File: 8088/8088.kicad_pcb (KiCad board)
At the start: 2 copper layers, 154.9 x 91.4 mm, 108 parts, among them CON1 BARREL_JACK, U1 8284, U10 2114, U11 ULN2803ADWR, U12 74LS14, U13 ULN2803ADWR, U14 ULN2803ADWR, U15 ULN2803ADWR, U16 7805, U2 8088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

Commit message: Updated libraries. Added IO headers to schematics. TODO: Route ISA bus
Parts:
- removed U3CLK/RDY: CONN_01X02, Pin_Headers:Pin_Header_Straight_1x02_Pitch2.54mm
- moved GND 5.71 mm to (223.0, 55.2)
- moved GND 5.71 mm to (216.7, 55.2)
- moved GND 5.71 mm to (210.2, 55.2)
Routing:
- net 8755-READY: track 6.02 -> 0.00 mm
- net 8755-CLK: track 4.07 -> 0.00 mm
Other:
- outline, holes or cut-outs redrawn
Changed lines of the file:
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@@
-(kicad_pcb (version 4) (host pcbnew 4.0.6)
+(kicad_pcb (version 4) (host pcbnew 4.0.3-stable)
   (general
-    (links 352)
+    (links 353)
     (no_connects 0)
     (area 62.23 19.05 255.270001 151.765001)
     (thickness 1.6)
     (drawings 7)
-    (tracks 1859)
+    (tracks 1855)
     (zones 0)
-    (modules 108)
+    (modules 107)
     (nets 189)
   )
@@
   )
   (module Pin_Headers:Pin_Header_Straight_2x02_Pitch2.54mm (layer F.Cu)
-    (at 223.012 49.53)
+    (at 223.012 55.245)
     (descr "Through hole straight pin header, 2x02, 2.54mm pitch, double rows")
     (tags "Through hole pin header THT 2x02 2.54mm double row")
@@
   )
   (module Pin_Headers:Pin_Header_Straight_2x02_Pitch2.54mm (layer F.Cu)
-    (at 216.662 49.53)
+    (at 216.662 55.245)
     (descr "Through hole straight pin header, 2x02, 2.54mm pitch, double rows")
     (tags "Through hole pin header THT 2x02 2.54mm double row")
@@
     )
   )
-  (module Pin_Headers:Pin_Header_Straight_1x02_Pitch2.54mm (layer F.Cu)
-    (at 139.7 69.85)
-    (descr "Through hole straight pin header, 1x02, 2.54mm pitch, single row")
-    (tags "Through hole pin header THT 1x02 2.54mm single row")
-    (fp_text reference U3CLK/RDY (at -2.54 1.27 90) (layer F.SilkS)
-      (effects (font (size 1 1) (thickness 0.15)))
-    )
-    (fp_text value CONN_01X02 (at 0 4.87) (layer F.Fab) hide
-      (effects (font (size 1 1) (thickness 0.15)))
-    )
-    (fp_line (start -0.635 -1.27) (end 1.27 -1.27) (layer F.Fab) (width 0.1))
-    (fp_line (start 1.27 -1.27) (end 1.27 3.81) (layer F.Fab) (width 0.1))
-    (fp_line (start 1.27 3.81) (end -1.27 3.81) (layer F.Fab) (width 0.1))
-    (fp_line (start -1.27 3.81) (end -1.27 -0.635) (layer F.Fab) (width 0.1))
-    (fp_line (start -1.27 -0.635) (end -0.635 -1.27) (layer F.Fab) (width 0.1))
-    (fp_line (start -1.33 3.87) (end 1.33 3.87) (layer F.SilkS) (width 0.12))
-    (fp_line (start -1.33 1.27) (end -1.33 3.87) (layer F.SilkS) (width 0.12))
-    (fp_line (start 1.33 1.27) (end 1.33 3.87) (layer F.SilkS) (width 0.12))
-    (fp_line (start -1.33 1.27) (end 1.33 1.27) (layer F.SilkS) (width 0.12))
-    (fp_line (start -1.33 0) (end -1.33 -1.33) (layer F.SilkS) (width 0.12))
-    (fp_line (start -1.33 -1.33) (end 0 -1.33) (layer F.SilkS) (width 0.12))
-    (fp_line (start -1.8 -1.8) (end -1.8 4.35) (layer F.CrtYd) (width 0.05))
-    (fp_line (start -1.8 4.35) (end 1.8 4.35) (layer F.CrtYd) (width 0.05))
-    (fp_line (start 1.8 4.35) (end 1.8 -1.8) (layer F.CrtYd) (width 0.05))
-    (fp_line (start 1.8 -1.8) (end -1.8 -1.8) (layer F.CrtYd) (width 0.05))
-    (fp_text user %R (at 0 1.27 90) (layer F.Fab)
-      (effects (font (size 1 1) (thickness 0.15)))
-    )
-    (pad 1 thru_hole rect (at 0 0) (size 1.7 1.7) (drill 1) (layers *.Cu *.Mask)
-      (net 86 8755-CLK))
-    (pad 2 thru_hole oval (at 0 2.54) (size 1.7 1.7) (drill 1) (layers *.Cu *.Mask)
-      (net 87 8755-READY))
-    (model ${KISYS3DMOD}/Pin_Headers.3dshapes/Pin_Header_Straight_1x02_Pitch2.54mm.wrl
-      (at (xyz 0 0 0))
-      (scale (xyz 1 1 1))
-      (rotate (xyz 0 0 0))
-    )
-  )
   (module Pin_Headers:Pin_Header_Straight_1x08_Pitch2.54mm (layer F.Cu)
     (at 162.56 83.82 180)
@@
   )
   (module Pin_Headers:Pin_Header_Straight_2x02_Pitch2.54mm (layer F.Cu)
-    (at 210.185 49.53)
+    (at 210.185 55.245)
     (descr "Through hole straight pin header, 2x02, 2.54mm pitch, double rows")
     (tags "Through hole pin header THT 2x02 2.54mm double row")
@@
   (gr_line (start 76.2 132.588) (end 76.2 41.148) (layer Edge.Cuts) (width 0.15))
   (gr_line (start 231.14 41.148) (end 231.14 132.588) (layer Edge.Cuts) (width 0.15))
-  (gr_line (start 220.98 41.148) (end 231.14 41.148) (layer Edge.Cuts) (width 0.15))
+  (gr_line (start 220.98 46.863) (end 231.14 46.863) (layer Edge.Cuts) (width 0.15))
   (gr_line (start 76.2 41.148) (end 220.98 41.148) (layer Edge.Cuts) (width 0.15))
   (segment (start 119.40806 48.641108) (end 119.323062 48.641108) (width 0.25) (layer B.Cu) (net 0))
@@
   (segment (start 160.587081 86.995) (end 159.88137 86.995) (width 0.1524) (layer B.Cu) (net 85))
   (segment (start 159.88137 86.995) (end 158.75 86.995) (width 0.1524) (layer B.Cu) (net 85))
-  (segment (start 139.7 69.85) (end 142.875 69.85) (width 0.1524) (layer F.Cu) (net 86))
-  (segment (start 142.875 69.85) (end 143.51 69.215) (width 0.1524) (layer F.Cu) (net 86))
-  (segment (start 139.7 72.39) (end 143.51 76.2) (width 0.1524) (layer F.Cu) (net 87))
-  (segment (start 143.51 76.2) (end 143.51 76.835) (width 0.1524) (layer F.Cu) (net 87))
   (segment (start 162.56 83.82) (end 159.385 83.82) (width 0.1524) (layer B.Cu) (net 88))
   (segment (start 159.385 83.82) (end 158.75 84.455) (width 0.1524) (layer B.Cu) (net 88))

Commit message: Second board revision down. Added bling :)
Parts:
- added D36: 1N914, Diodes_ThroughHole:D_DO-35_SOD27_P2.54mm_Vertical_AnodeUp, F.Cu at (111.1, 125.5)
- added D37: 1N914, Diodes_ThroughHole:D_DO-35_SOD27_P2.54mm_Vertical_AnodeUp, F.Cu at (104.8, 125.5)
- added JP2: JUMPER3, Pin_Headers:Pin_Header_Straight_1x03_Pitch2.54mm, F.Cu at (105.4, 119.9)
- added P10: CONN_01X15, Pin_Headers:Pin_Header_Straight_1x15_Pitch2.54mm, F.Cu at (109.9, 102.2)
- added P11: CONN_01X05, Pin_Headers:Pin_Header_Straight_1x05_Pitch2.54mm, F.Cu at (134.6, 80.6)
- added P12: CONN_01X05, Pin_Headers:Pin_Header_Straight_1x05_Pitch2.54mm, F.Cu at (134.6, 66.9)
- added P13: CONN_01X08, Pin_Headers:Pin_Header_Straight_1x08_Pitch2.54mm, F.Cu at (140.5, 132.5)
- added P14: CONN_01X08, Pin_Headers:Pin_Header_Straight_1x08_Pitch2.54mm, F.Cu at (132.2, 132.5)
- added P9: CONN_01X06, Pin_Headers:Pin_Header_Straight_1x06_Pitch2.54mm, F.Cu at (228.6, 91.9)
- added REF**: MountingHole_2.2mm_M2, Mounting_Holes:MountingHole_2.2mm_M2, F.Cu at (80.0, 54.6)
- added REF**: MountingHole_2.2mm_M2, Mounting_Holes:MountingHole_2.2mm_M2, F.Cu at (227.3, 54.6)
- added REF**: MountingHole_2.2mm_M2, Mounting_Holes:MountingHole_2.2mm_M2, F.Cu at (227.3, 115.6)
- added REF**: MountingHole_2.2mm_M2, Mounting_Holes:MountingHole_2.2mm_M2, F.Cu at (80.0, 115.6)
- added REF***: OSHW-Logo_11.4x12mm_SilkScreen, Symbols:OSHW-Logo_11.4x12mm_SilkScreen, F.Cu at (88.9, 47.6)
- added REF***: KiCad-Logo2_6mm_SilkScreen, Symbols:KiCad-Logo2_6mm_SilkScreen, F.Cu at (223.5, 130.2)
- added U8: 8282, Housings_DIP:DIP-20_W7.62mm_Socket, F.Cu at (140.3, 128.5)
- moved GND 10.2 mm to (223.0, 45.1)
- moved GND 10.2 mm to (216.7, 45.1)
- moved GND 10.2 mm to (210.2, 45.1)
- moved D1 4.66 mm to (108.0, 125.5)
- moved PWR 4.08 mm to (98.2, 128.7)
- moved 7-25V 2.40 mm to (85.5, 123.8)
- renumbered CON1 to 7-25V
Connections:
- net 8755-CLK renamed Net-(U3-Pad3)
- net 8755-READY renamed Net-(U3-Pad6)
- net Net-(R4-Pad1) renamed /~IOR
- net Net-(U12-Pad1) renamed /DEC5
- net Net-(U2-Pad25) renamed /ALE
- net Net-(U4-Pad8) renamed /DEC6
- net Net-(U5-Pad11) renamed /DEC7
- net Net-(U6-Pad5) renamed /DEC0
- U5 pad 14: Net-(U5-Pad14) -> /RXRDY
- U5 pad 17: GND -> /~CTS
- U5 pad 18: Net-(U5-Pad18) -> /TXEMP
- U5 pad 22: Net-(U5-Pad22) -> /~DSR
- U5 pad 23: Net-(U5-Pad23) -> /~RTS
- U5 pad 24: Net-(U5-Pad24) -> /~DTR
- U7 pad 11: Net-(U7-Pad11) -> /DEC4
- U7 pad 12: Net-(U7-Pad12) -> /DEC3
- U7 pad 13: Net-(U7-Pad13) -> /DEC2
- U7 pad 14: Net-(U7-Pad14) -> /DEC1
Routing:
- net /A0: track 92.3 -> 189.9 mm, vias 3 -> 8
- net /A1: track 88.3 -> 168.8 mm, vias 2 -> 4
- net /A5: track 91.4 -> 167.5 mm, vias 3 -> 8
- net /A2: track 93.3 -> 168.3 mm, vias 1 -> 4
- net /A7: track 76.6 -> 150.6 mm, vias 1 -> 3
- net /A3: track 84.1 -> 156.8 mm, vias 1 -> 4
- net /A4: track 84.3 -> 148.9 mm, vias 1 -> 3
- net /A6: track 84.0 -> 136.5 mm, vias 1 -> 4
- net /AD1: track 195.6 -> 247.1 mm, vias 3 -> 5
- net /AD4: track 230.6 -> 281.1 mm, vias 9 -> 14
- net /AD2: track 193.6 -> 237.3 mm, vias 4 -> 6
- net /AD0: track 198.6 -> 241.1 mm, vias 5 -> 8
- net /~DTR: track 0.00 -> 37.8 mm, vias 0 -> 2
- net /ALE: track 60.5 -> 96.6 mm, vias 2 -> 3
- net /AD3: track 214.9 -> 250.3 mm
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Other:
- board size 154.9 x 91.4 mm -> 154.9 x 93.5 mm
- board text added: "A0"
- board text added: "A10"
- board text added: "A11"
- board text added: "A12"
- board text added: "A13"
- board text added: "A14"
- board text added: "A15"
- board text added: "A16"
- board text added: "A17"
- board text added: "A18"
- board text added: "A19"
- board text added: "A7"
- board text added: "A8"
- board text added: "A9"
- board text added: "AD0"
- board text added: "AD1"
- board text added: "AD2"
- board text added: "AD3"
- board text added: "AD4"
- board text added: "AD5"
- board text added: "AD6"
- board text added: "AD7"
- board text added: "DEC0"
- board text added: "DEC7"
- board text added: "ECLK"
- board text added: "M2"
- board text added: "Neo ECK-88 Bryan Orabutt 2017"
- board text added: "PA0"
- board text added: "PA1"
- board text added: "PA2"
- board text added: "PA3"
- board text added: "PA4"
- board text added: "PA5"
- board text added: "PA6"
- board text added: "PA7"
- board text added: "PB"
- board text added: "PB0"
- board text added: "PB1"
- board text added: "PB2"
- board text added: "PB3"
- board text added: "PB4"
- board text added: "PB5"
- board text added: "PB6"
- board text added: "PB7"
- board text added: "PC0"
- board text added: "PC1"
- board text added: "PC2"
- board text added: "PC3"
- board text added: "PC4"
- board text added: "PC5"
- board text added: "RX"
- board text added: "RXRDY"
- board text added: "SYS_CLK"
- board text added: "TX"
- board text added: "TXEMPTY"
- board text added: "~ALE"
- board text added: "~CTS"
- board text added: "~DSR"
- board text added: "~DTR"
- board text added: "~IOR"
- board text added: "~M"
- board text added: "~RD"
- board text added: "~RTS"
- board text added: "~WR"

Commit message: Added gerbers.
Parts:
- added REF**: via-0.7mm, Library:via-0.7mm, F.Cu at (82.3, 128.5)
- added REF**: via-0.7mm, Library:via-0.7mm, F.Cu at (86.1, 126.5)
- added REF**: via-0.7mm, Library:via-0.7mm, F.Cu at (87.4, 126.5)
- added REF**: via-0.7mm, Library:via-0.7mm, F.Cu at (88.6, 126.5)
- added REF**: via-0.7mm, Library:via-0.7mm, F.Cu at (88.6, 124.5)
- added REF**: via-0.7mm, Library:via-0.7mm, F.Cu at (87.4, 124.5)
- added REF**: via-0.7mm, Library:via-0.7mm, F.Cu at (86.1, 124.5)
- added REF**: via-0.7mm, Library:via-0.7mm, F.Cu at (84.8, 124.5)
- added REF**: via-0.7mm, Library:via-0.7mm, F.Cu at (83.6, 124.5)
- added REF**: via-0.7mm, Library:via-0.7mm, F.Cu at (83.6, 128.5)
- added REF**: via-0.7mm, Library:via-0.7mm, F.Cu at (82.3, 124.5)
- added REF**: via-0.7mm, Library:via-0.7mm, F.Cu at (84.8, 128.5)
- added REF**: via-0.7mm, Library:via-0.7mm, F.Cu at (86.1, 128.5)
- added REF**: via-0.7mm, Library:via-0.7mm, F.Cu at (87.4, 128.5)
- added REF**: via-0.7mm, Library:via-0.7mm, F.Cu at (88.6, 128.5)
- added REF**: via-0.7mm, Library:via-0.7mm, F.Cu at (82.3, 126.5)
- added REF**: via-0.7mm, Library:via-0.7mm, F.Cu at (83.6, 126.5)
- added REF**: via-0.7mm, Library:via-0.7mm, F.Cu at (84.8, 126.5)
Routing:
- net GND: track 76.8 -> 64.4 mm, vias 9 -> 3
- added copper zone on F.Cu, net GND

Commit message: Reformatted README
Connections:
- JP2 pad 1: Net-(JP2-Pad1) -> GND
- JP2 pad 3: Net-(JP2-Pad3) -> GND

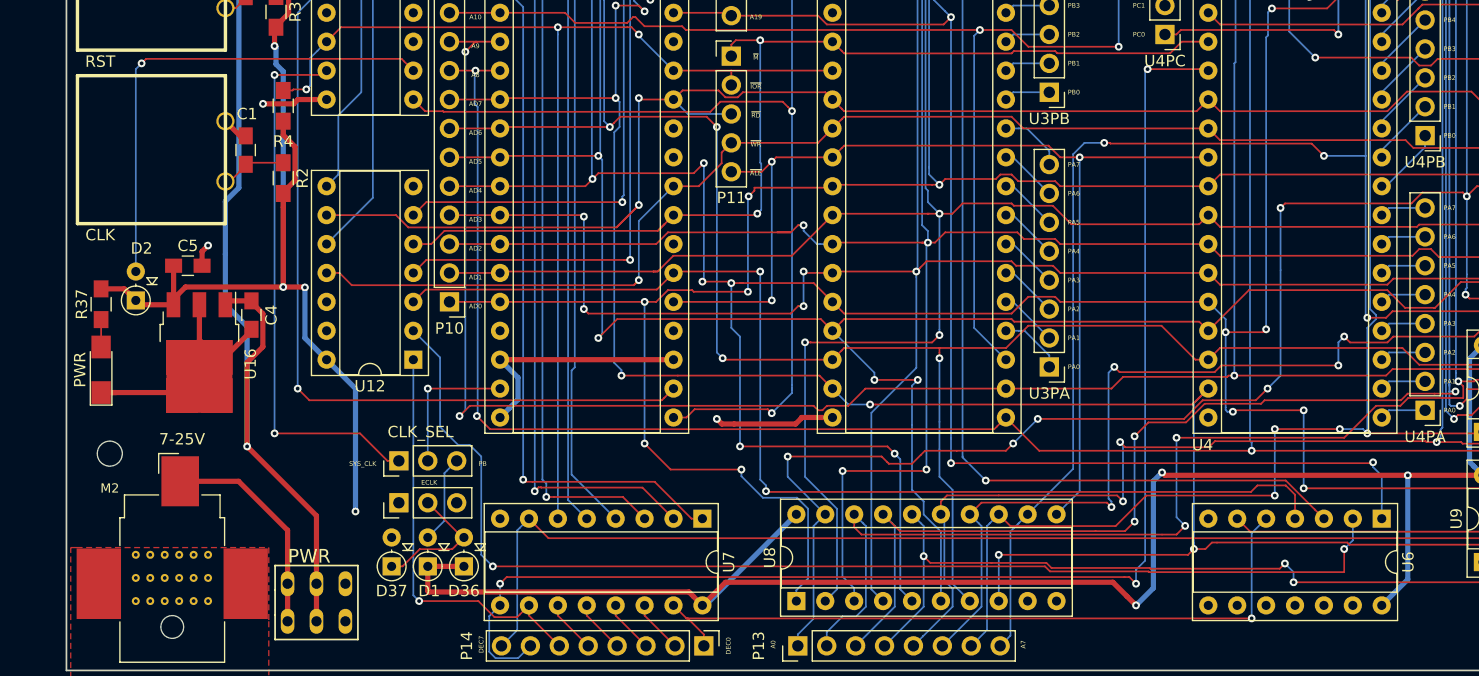
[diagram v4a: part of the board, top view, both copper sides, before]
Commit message: Changed regulator
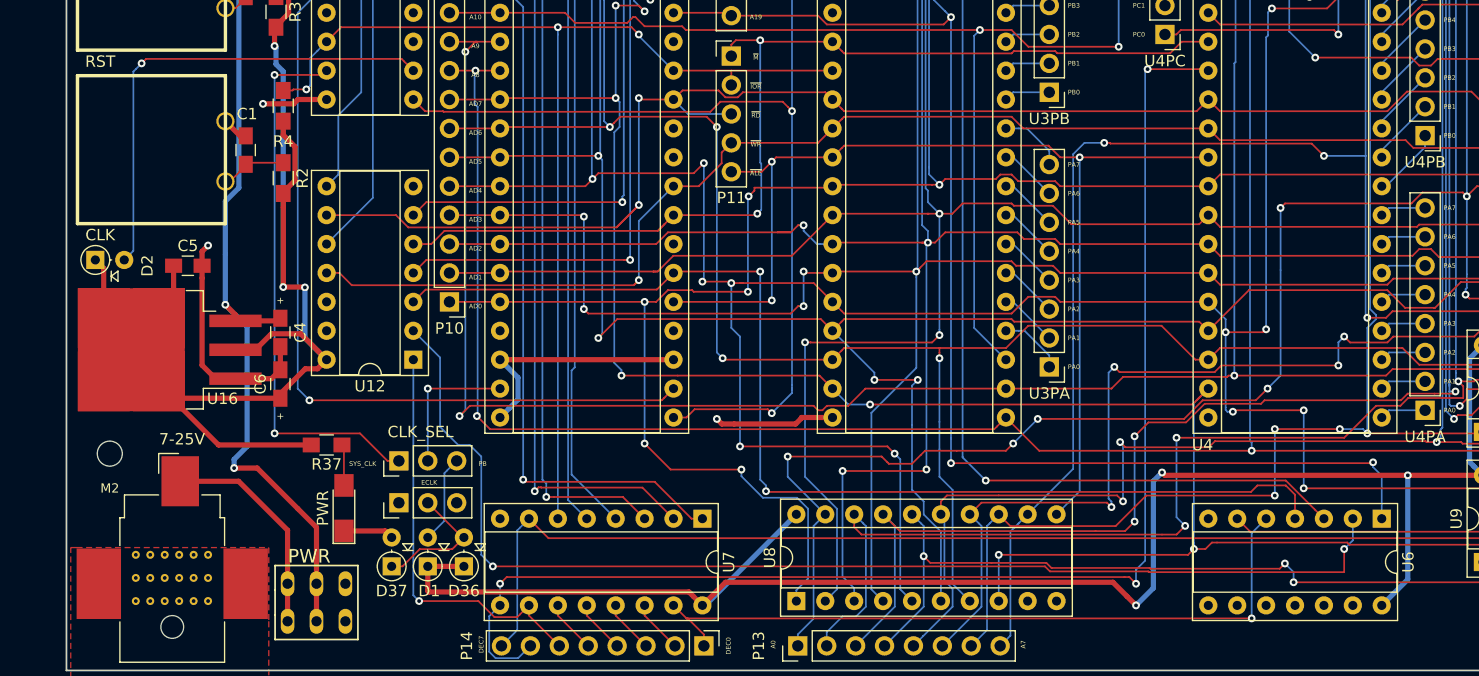
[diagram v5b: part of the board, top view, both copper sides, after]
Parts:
- added C6: 10uF, Capacitors_SMD:C_0805_HandSoldering, F.Cu at (95.0, 109.5)
- C4: value 1uF -> 10uF
- U16: value 7805 -> LM1084IT-5.0/NOPB; footprint TO_SOT_Packages_SMD:TO-252-3_TabPin2 -> TO_SOT_Packages_SMD:TO-263-3_TabPin2
- moved PWR 24.6 mm to (100.6, 120.4)
- moved R37 23.4 mm to (99.1, 114.8), turned to 180 degrees
- moved D2 5.03 mm to (78.7, 98.6), turned to 0 degrees
- moved C4 2.96 mm to (95.0, 104.9)
- moved U16 2.62 mm to (85.3, 106.4), turned to 180 degrees
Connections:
- JP2 pad 1: GND -> Net-(JP2-Pad1)
- JP2 pad 3: GND -> Net-(JP2-Pad3)
- U10 pad 8: Net-(U10-Pad8) -> (no net)
- U16 pad 1: /P_IN -> GND
- U16 pad 2: GND -> +5V
- U16 pad 3: +5V -> /P_IN
- U6 pad 6: Net-(U10-Pad8) -> Net-(U10-Pad~)
- U9 pad 8: Net-(U10-Pad8) -> (no net)
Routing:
- net Net-(U10-Pad~): track 0.00 -> 53.4 mm, vias 0 -> 1
- net Net-(U10-Pad8): track 53.4 -> 0.00 mm, vias 1 -> 0
- net +5V: track 455.0 -> 472.6 mm, vias 13 -> 12
- net /P_IN: track 385.5 -> 377.3 mm, vias 7 -> 8
- net GND: track 64.4 -> 67.7 mm
- net Net-(D35-Pad2): track 2.41 -> 3.63 mm
- net Net-(D2-Pad2): track 43.0 -> 42.4 mm
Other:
- board text added: "+"

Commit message: Updated board layout
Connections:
- U10 pad 8: (no net) -> Net-(U10-Pad8)
- U6 pad 6: Net-(U10-Pad~) -> Net-(U10-Pad8)
- U9 pad 8: (no net) -> Net-(U10-Pad8)
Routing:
- net Net-(U10-Pad~): track 53.4 -> 0.00 mm, vias 1 -> 0
- net Net-(U10-Pad8): track 0.00 -> 53.4 mm, vias 0 -> 1
